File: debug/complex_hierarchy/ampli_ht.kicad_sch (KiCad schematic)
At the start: 29 parts, among them P3 CONN_2, P4 CONN_2, Q1 MPSA92, Q2 MPSA42, Q3 MPSA92, Q4 MPSA42, U3 LM358N

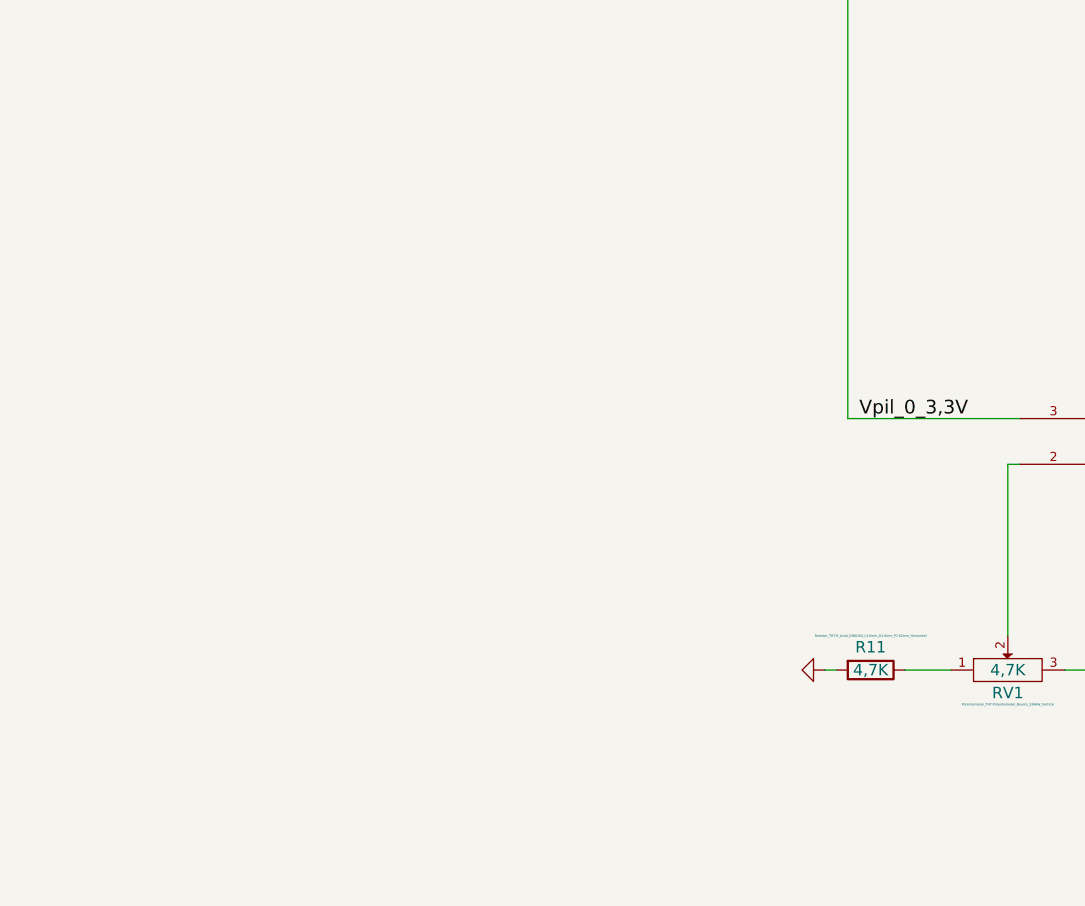
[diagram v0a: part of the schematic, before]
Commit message: Trying to fix the table header
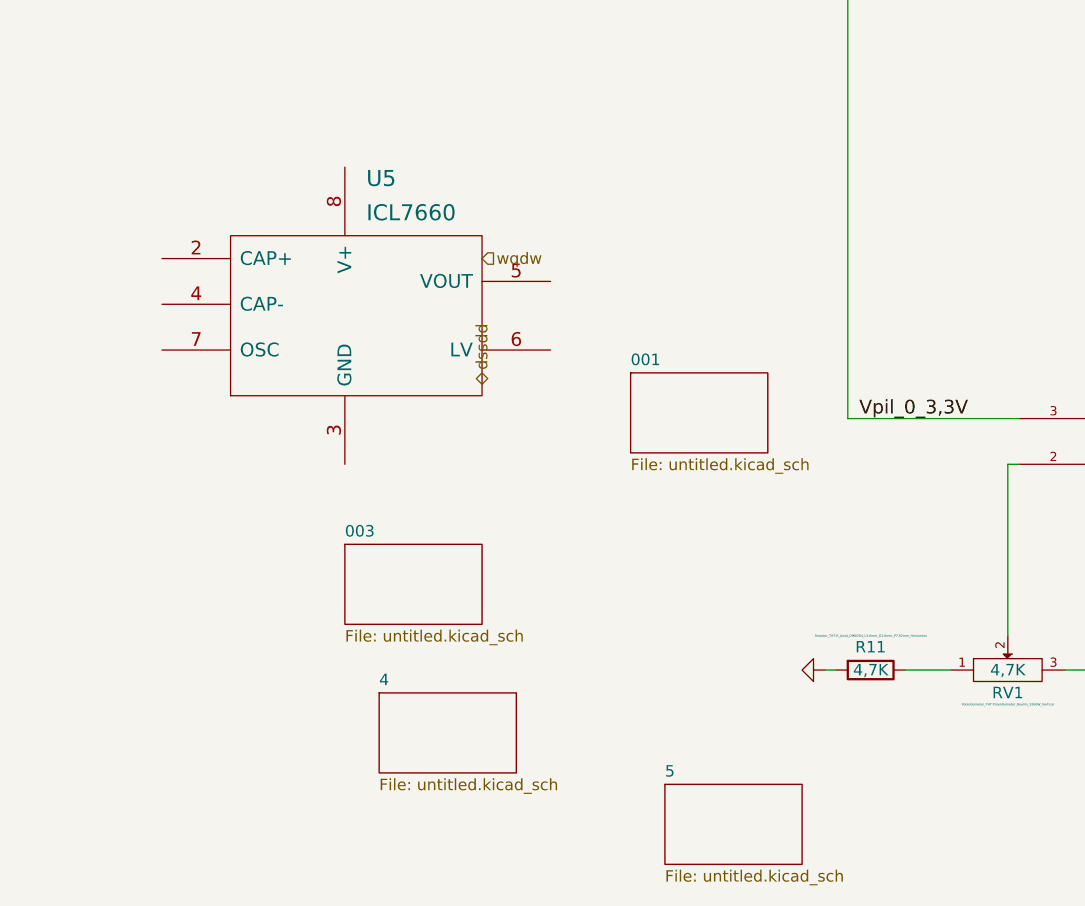
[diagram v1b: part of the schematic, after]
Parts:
- added U5: ICL7660, symbol complex_hierarchy_schlib:ICL7660
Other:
- added sheet 001 (untitled.kicad_sch)
- added sheet 003 (untitled.kicad_sch)
- added sheet 4 (untitled.kicad_sch)
- added sheet 5 (untitled.kicad_sch)
